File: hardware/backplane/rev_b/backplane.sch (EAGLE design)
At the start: 345 parts, among them J0 BACKPLANE_GENERIC_MODULE, J1 BACKPLANE_GENERIC_MODULE, J2 BACKPLANE_GENERIC_MODULE, J3 BACKPLANE_CONTROLLER_MODULE, J4 BACKPLANE_POWER_MODULE, J5 BACKPLANE_GENERIC_MODULE, J6 BACKPLANE_GENERIC_MODULE, J7 BACKPLANE_GENERIC_MODULE, J8 SCREW_TERMINAL, J9 SCREW_TERMINAL, U1 TUSB2077A, U10 SN74LVC2T45, U11 SN74LVC2T45, U12 SN74LVC2T45, U13 SN74LVC2T45, U14 SN74LVC2T45, U15 SN74LVC2T45, U16 SN74LVC2T45, U17 SN74LVC2T45, U18 SN74LVC2T45, U19 SN74LVC2T45, U2 FXMA2102, U20 TS3USB30E, U21 TS3USB30E, U22 TS3USB30E, U23 TS3USB30E, U24 TS3USB30E, U25 TS3USB30E, U26 MCP23008, U27 MCP23008, U28 MCP23008, U29 MCP23008, U3 FXMA2102, U30 MCP23008, U31 MCP23008, U4 FXMA2102, U5 FXMA2102, U6 FXMA2102, U7 FXMA2102, U8 SN74LVC2T45, U9 SN74LVC2T45, Y1 ABMM

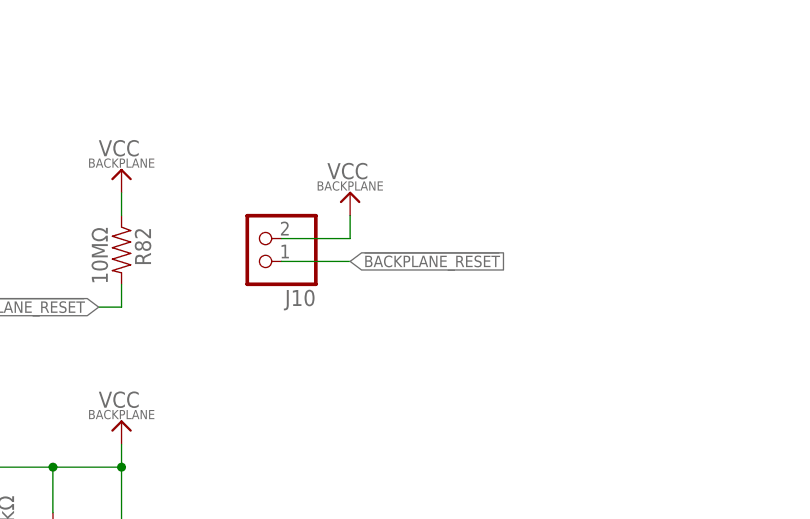
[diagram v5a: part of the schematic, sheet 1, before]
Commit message: Remove `!BACKPLANE_RESET` header b/c pulled up now
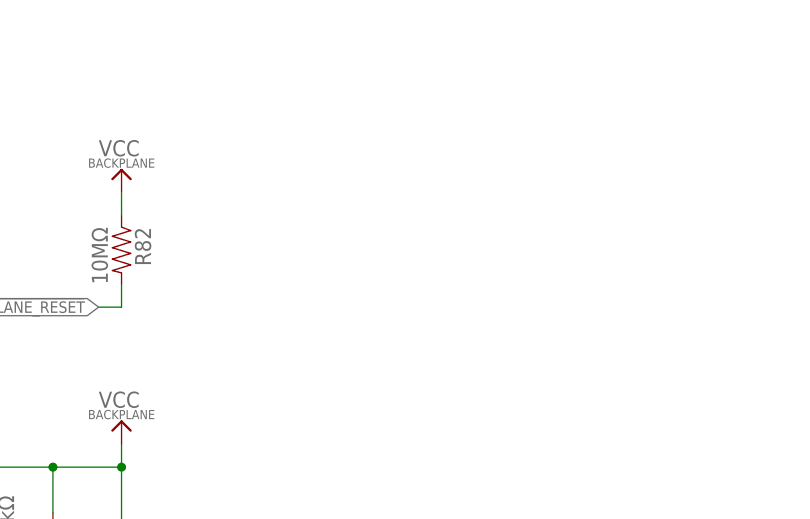
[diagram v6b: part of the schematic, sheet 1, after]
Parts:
- removed J10: (no value), pinhead:PINHD-1X2
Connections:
- net !BACKPLANE_RESET: no longer J10.1
- net VCC_BACKPLANE: no longer J10.2
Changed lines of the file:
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@@
 <part name="TP31" library="headers" deviceset="TEST_POINT_0.040IN" device=""/>
 <part name="TP10" library="headers" deviceset="TEST_POINT_0.040IN" device=""/>
-<part name="J10" library="pinhead" deviceset="PINHD-1X2" device=""/>
-<part name="U$51" library="signpost" deviceset="VCC_BACKPLANE" device=""/>
 <part name="R62" library="passives" deviceset="RESISTOR" device="0603_RES" value="15kΩ"/>
 <part name="R63" library="passives" deviceset="RESISTOR" device="0603_RES" value="15kΩ"/>
@@
 <instance part="J9" gate="G$1" x="190.5" y="50.8" rot="R180"/>
 <instance part="LOGO1" gate="G$1" x="2.54" y="172.72"/>
-<instance part="J10" gate="G$1" x="177.8" y="160.02" rot="R180"/>
-<instance part="U$51" gate="G$1" x="187.96" y="162.56"/>
 <instance part="U$52" gate="G$1" x="162.56" y="165.1"/>
 </instances>
@@
 </segment>
 <segment>
-<pinref part="J10" gate="G$1" pin="2"/>
-<pinref part="U$51" gate="G$1" pin="VCC_BACKPLANE"/>
-<wire x1="180.34" y1="160.02" x2="187.96" y2="160.02" width="0.1524" layer="91"/>
-<wire x1="187.96" y1="160.02" x2="187.96" y2="162.56" width="0.1524" layer="91"/>
-</segment>
-<segment>
 <pinref part="R82" gate="G$1" pin="1"/>
 <pinref part="U$52" gate="G$1" pin="VCC_BACKPLANE"/>
@@
 <label x="160.02" y="152.4" size="1.27" layer="95" rot="R180" xref="yes"/>
 </segment>
-<segment>
-<pinref part="J10" gate="G$1" pin="1"/>
-<wire x1="187.96" y1="157.48" x2="180.34" y2="157.48" width="0.1524" layer="91"/>
-<label x="187.96" y="157.48" size="1.27" layer="95" xref="yes"/>
-</segment>
-</net>
+</net>

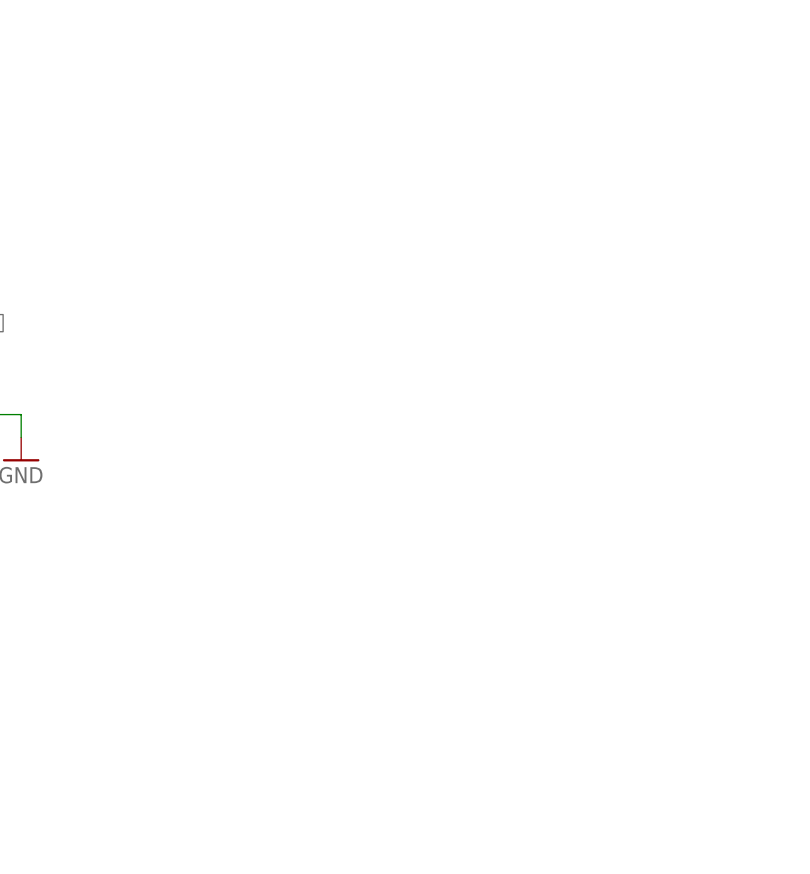
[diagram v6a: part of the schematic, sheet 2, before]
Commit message: backplane: Add labels to modules
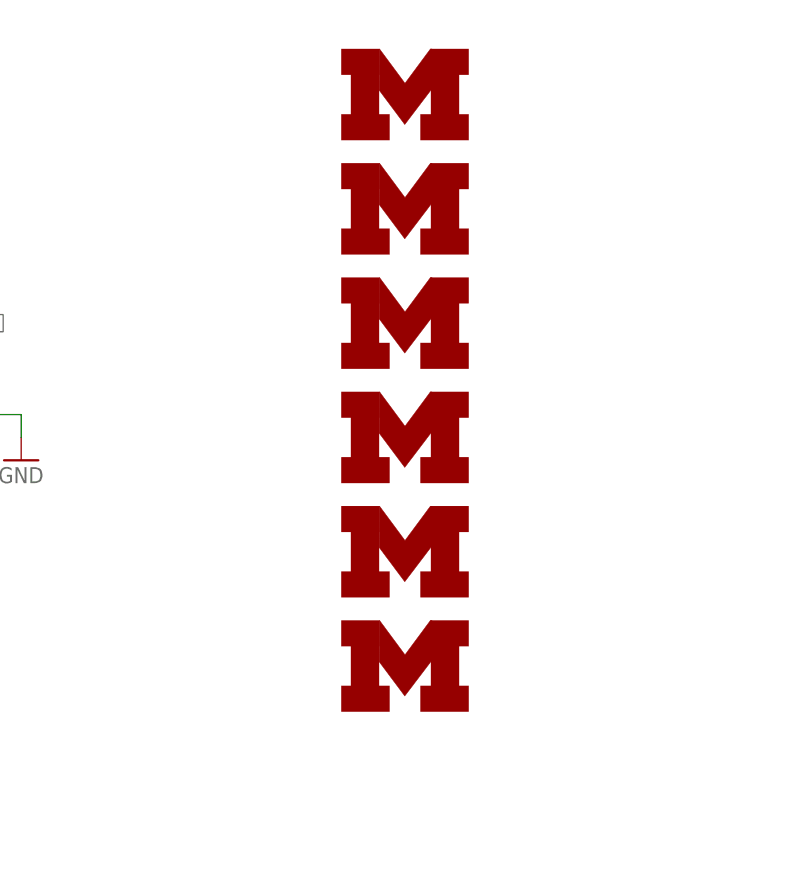
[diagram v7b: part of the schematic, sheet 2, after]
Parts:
- added LOGO2, LOGO3, LOGO4, LOGO5, LOGO6, LOGO7, LOGO8, LOGO9: UMICH_SOLID_MEDIUM, logos:UMICH_SOLID_MEDIUM
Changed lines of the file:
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@@
 <part name="GND142" library="umich" deviceset="GND" device=""/>
 <part name="U$52" library="signpost" deviceset="VCC_BACKPLANE" device=""/>
+<part name="LOGO2" library="logos" deviceset="UMICH_SOLID" device="_MEDIUM"/>
+<part name="LOGO3" library="logos" deviceset="UMICH_SOLID" device="_MEDIUM"/>
+<part name="LOGO4" library="logos" deviceset="UMICH_SOLID" device="_MEDIUM"/>
+<part name="LOGO5" library="logos" deviceset="UMICH_SOLID" device="_MEDIUM"/>
+<part name="LOGO6" library="logos" deviceset="UMICH_SOLID" device="_MEDIUM"/>
+<part name="LOGO7" library="logos" deviceset="UMICH_SOLID" device="_MEDIUM"/>
+<part name="LOGO8" library="logos" deviceset="UMICH_SOLID" device="_MEDIUM"/>
+<part name="LOGO9" library="logos" deviceset="UMICH_SOLID" device="_MEDIUM"/>
 </parts>
 <sheets>
@@
 <instance part="LOGO1" gate="G$1" x="2.54" y="172.72"/>
 <instance part="U$52" gate="G$1" x="162.56" y="165.1"/>
+<instance part="LOGO8" gate="G$1" x="15.24" y="132.08"/>
+<instance part="LOGO9" gate="G$1" x="15.24" y="53.34"/>
 </instances>
 <busses>
@@
 <instance part="GND28" gate="1" x="127" y="2.54"/>
 <instance part="GND29" gate="1" x="127" y="50.8"/>
+<instance part="LOGO2" gate="G$1" x="162.56" y="170.18"/>
+<instance part="LOGO3" gate="G$1" x="162.56" y="157.48"/>
+<instance part="LOGO4" gate="G$1" x="162.56" y="144.78"/>
+<instance part="LOGO5" gate="G$1" x="162.56" y="132.08"/>
+<instance part="LOGO6" gate="G$1" x="162.56" y="119.38"/>
+<instance part="LOGO7" gate="G$1" x="162.56" y="106.68"/>
 </instances>
 <busses>

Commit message: backplane: add hole for power module
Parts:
- removed J8, J9: SCREW_TERMINAL, connector:SCREW_TERMINAL
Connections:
- net VBATT+: no longer J9.1
- net VBATT-: no longer J9.2
- net VSOL+: no longer J8.1
- net VSOL-: no longer J8.2
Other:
- note removed: "!!! Placeholder until Josh gets real connectors !!!"
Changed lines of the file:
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@@
 <part name="C13" library="passives" deviceset="CAPACITOR" device="0402_CAP" value="22pF"/>
 <part name="C14" library="passives" deviceset="CAPACITOR" device="0402_CAP" value="22pF"/>
-<part name="J8" library="connector" deviceset="SCREW_TERMINAL" device=""/>
-<part name="J9" library="connector" deviceset="SCREW_TERMINAL" device=""/>
 <part name="C22" library="passives" deviceset="CAPACITOR" device="0603_CAP" value="100nF"/>
 <part name="C24" library="passives" deviceset="CAPACITOR" device="0603_CAP" value="100nF"/>
@@
 <text x="246.38" y="182.88" size="5.08" layer="98" align="top-right">Special Modules</text>
 <text x="147.32" y="175.26" size="2.54" layer="98" align="center">Pull-up/downs</text>
-<text x="147.32" y="25.4" size="6.4516" layer="98">!!! Placeholder until Josh
-gets real connectors !!!</text>
 </plain>
 <instances>
@@
 <instance part="R48" gate="G$1" x="154.94" y="99.06" rot="R90"/>
 <instance part="R49" gate="G$1" x="162.56" y="96.52" rot="R90"/>
-<instance part="J8" gate="G$1" x="190.5" y="68.58" rot="R180"/>
-<instance part="J9" gate="G$1" x="190.5" y="50.8" rot="R180"/>
 <instance part="LOGO1" gate="G$1" x="2.54" y="172.72"/>
 <instance part="U$52" gate="G$1" x="162.56" y="165.1"/>
@@
 <label x="71.12" y="83.82" size="1.27" layer="95" xref="yes"/>
 </segment>
-<segment>
-<pinref part="J8" gate="G$1" pin="1"/>
-<wire x1="182.88" y1="71.12" x2="185.42" y2="71.12" width="0.1524" layer="91"/>
-<label x="182.88" y="71.12" size="1.27" layer="95" rot="R180" xref="yes"/>
-</segment>
 </net>
 <net name="VSOL-" class="0">
@@
 <label x="71.12" y="81.28" size="1.27" layer="95" xref="yes"/>
 </segment>
-<segment>
-<pinref part="J8" gate="G$1" pin="2"/>
-<wire x1="182.88" y1="66.04" x2="185.42" y2="66.04" width="0.1524" layer="91"/>
-<label x="182.88" y="66.04" size="1.27" layer="95" rot="R180" xref="yes"/>
-</segment>
 </net>
 <net name="VBATT+" class="0">
@@
 <label x="71.12" y="78.74" size="1.27" layer="95" xref="yes"/>
 </segment>
-<segment>
-<pinref part="J9" gate="G$1" pin="1"/>
-<wire x1="182.88" y1="53.34" x2="185.42" y2="53.34" width="0.1524" layer="91"/>
-<label x="182.88" y="53.34" size="1.27" layer="95" rot="R180" xref="yes"/>
-</segment>
 </net>
 <net name="VBATT-" class="0">
@@
 <label x="71.12" y="76.2" size="1.27" layer="95" xref="yes"/>
 </segment>
-<segment>
-<pinref part="J9" gate="G$1" pin="2"/>
-<wire x1="182.88" y1="48.26" x2="185.42" y2="48.26" width="0.1524" layer="91"/>
-<label x="182.88" y="48.26" size="1.27" layer="95" rot="R180" xref="yes"/>
-</segment>
-</net>
+</net>
